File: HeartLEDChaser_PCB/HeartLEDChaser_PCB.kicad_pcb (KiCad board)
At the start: 2 copper layers, 58.8 x 52.2 mm, 35 parts, among them U1 ICM7555CBAZ, U2 CD4017BM, U3 HT7750A, U4 HX SS12F44G4

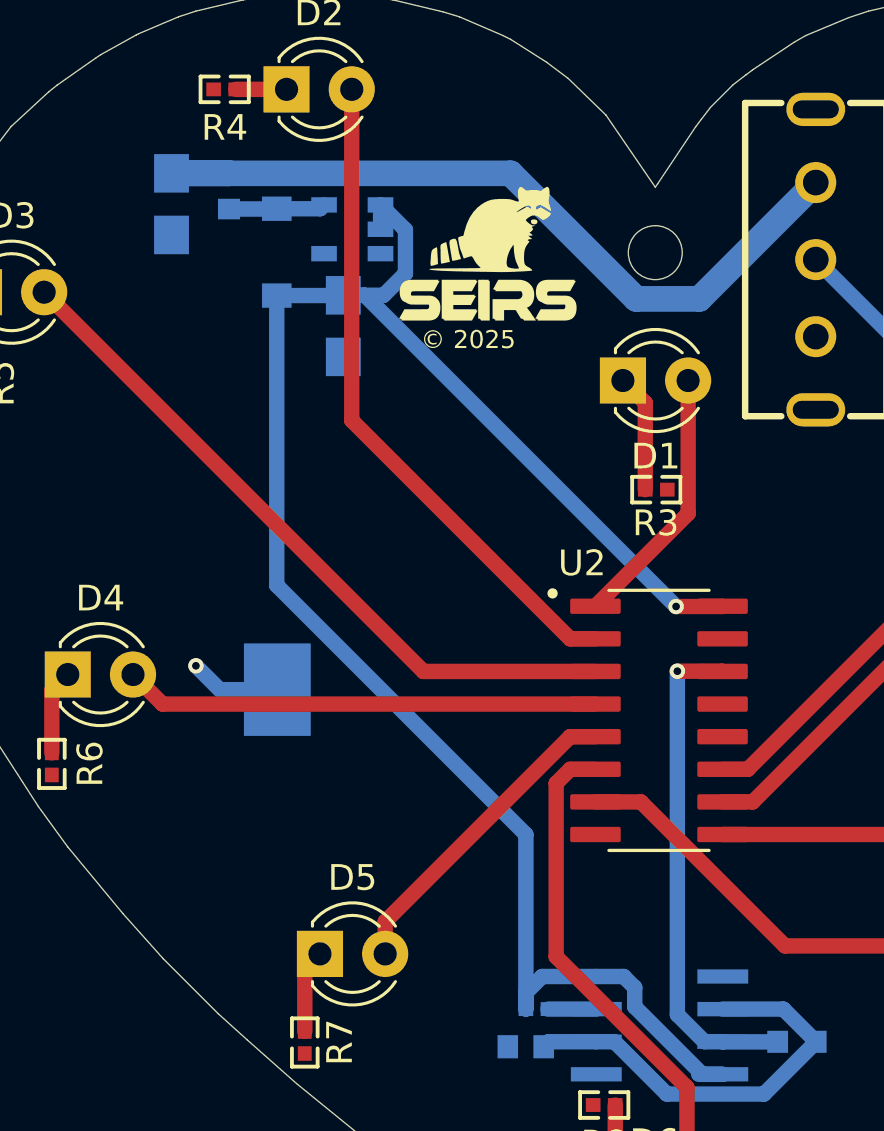
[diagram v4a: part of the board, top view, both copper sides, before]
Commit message: Corrected capacitor references
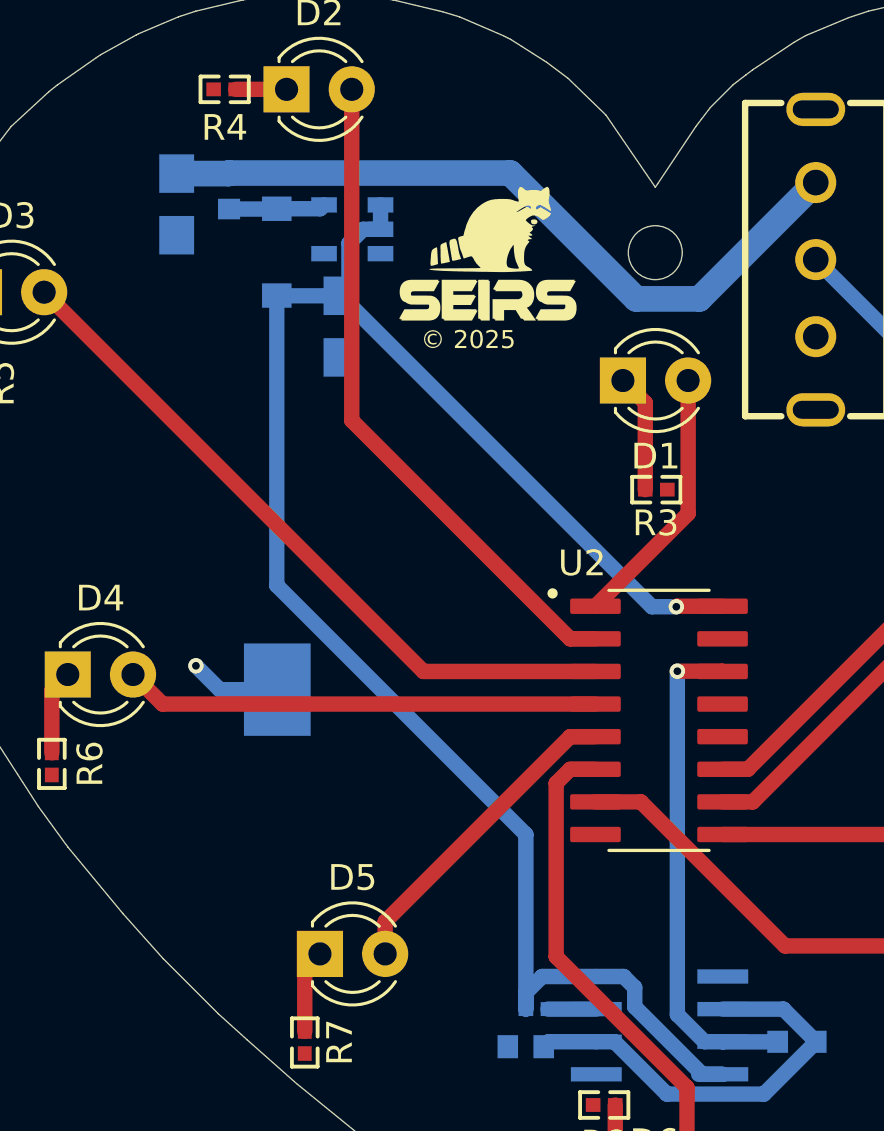
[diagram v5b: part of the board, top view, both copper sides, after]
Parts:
- removed C4: 22uF(Tantalum), FOOTPRINTS:TAJA476K006RNJ
- added C2: 47uF(Tantalum), FOOTPRINTS:TAJA476K006RNJ, B.Cu at (111.4, 80.7)
- C3: value 47uF(Tantalum) -> 22uF(Tantalum)
- moved C3 8.14 mm to (117.8, 85.5)
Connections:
- C3 pad 1: +3V0 -> +5V
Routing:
- net +3V0: track 31.2 -> 28.8 mm
- net +5V: track 72.5 -> 70.3 mm
- net Net-(D5-K): track 3.26 -> 2.43 mm
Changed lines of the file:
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@@
 	(footprint "FOOTPRINTS:TAJA476K006RNJ"
 		(layer "B.Cu")
-		(at 111.16 80.71 -90)
-		(property "Reference" "C3"
-			(at -0.01 1.64 -90)
+		(at 111.36 80.72 -90)
+		(property "Reference" "C2"
+			(at -0.01 1.69 90)
 			(layer "B.SilkS")
 			(effects
@@
 		)
 	)
-	(footprint "FOOTPRINTS:TAJA476K006RNJ"
-		(layer "B.Cu")
-		(at 117.85 85.46 -90)
-		(property "Reference" "C4"
-			(at 2.92 0.02 0)
-			(layer "B.SilkS")
-			(effects
-				(font
-					(size 1 1)
-					(thickness 0.15)
-				)
-				(justify mirror)
-			)
-		)
-		(property "Value" "22uF(Tantalum)"
-			(at 0 -4 90)
-			(layer "B.Fab")
-			(effects
-				(font
-					(size 1 1)
-					(thickness 0.15)
-				)
-				(justify mirror)
-			)
-		)
-		(property "Footprint" "FOOTPRINTS:TAJA476K006RNJ"
-			(at 0 0 90)
-			(layer "B.Fab")
-			(hide yes)
-			(effects
-				(font
-					(size 1.27 1.27)
-					(thickness 0.15)
-				)
-				(justify mirror)
-			)
-		)
-		(property "Datasheet" ""
-			(at 0 0 90)
-			(layer "B.Fab")
-			(hide yes)
-			(effects
-				(font
-					(size 1.27 1.27)
-					(thickness 0.15)
-				)
-				(justify mirror)
-			)
-		)
-		(property "Description" "Polarized capacitor"
-			(at 0 0 90)
-			(layer "B.Fab")
-			(hide yes)
-			(effects
-				(font
-					(size 1.27 1.27)
-					(thickness 0.15)
-				)
-				(justify mirror)
-			)
-		)
-		(property ki_fp_filters "CP_*")
-		(sheetname "Root")
-		(sheetfile "HeartLEDChaser_PCB.kicad_sch")
-		(attr smd)
-		(fp_line
-			(start -0.32 0.8)
-			(end -0.32 -0.8)
-			(stroke
-				(width 0.08)
-				(type solid)
-			)
-			(layer "B.SilkS")
-		)
-		(fp_line
-			(start 1.6 0.8)
-			(end -1.6 0.8)
-			(stroke
-				(width 0.08)
-				(type solid)
-			)
-			(layer "B.SilkS")
-		)
-		(fp_line
-			(start 1.57 -0.8)
-			(end -1.58 -0.8)
-			(stroke
-				(width 0.08)
-				(type solid)
-			)
-			(layer "B.SilkS")
-		)
-		(fp_circle
-			(center -1.6 -0.8)
-			(end -1.57 -0.8)
-			(stroke
-				(width 0.06)
-				(type solid)
-			)
-			(fill none)
-			(layer "B.Fab")
-		)
-		(fp_text user "${REFERENCE}"
-			(at 0 0 90)
-			(layer "B.Fab")
-			(effects
-				(font
-					(size 1 1)
-					(thickness 0.15)
-				)
-				(justify mirror)
-			)
-		)
-		(pad "1" smd rect
-			(at -1.2 0 270)
-			(size 1.5 1.36)
-			(layers "B.Cu" "B.Paste" "B.Mask")
-			(net 34 "+5V")
-			(pintype "passive")
-		)
-		(pad "2" smd rect
-			(at 1.2 0 270)
-			(size 1.5 1.36)
-			(layers "B.Cu" "B.Paste" "B.Mask")
-			(net 2 "GND")
-			(pintype "passive")
-		)
-		(model "${EASYEDA2KICAD}/easyeda2kicad.3dshapes/CASE-A_L3.2-W1.6-H1.6.wrl"
-			(offset
-				(xyz -0 -0 -0)
-			)
-			(scale
-				(xyz 1 1 1)
-			)
-			(rotate
-				(xyz 0 0 0)
-			)
-		)
-	)
 	(footprint "FOOTPRINTS:CL10A475KP8NNNC"
 		(layer "B.Cu")
@@
 		)
 	)
+	(footprint "FOOTPRINTS:TAJA476K006RNJ"
+		(layer "B.Cu")
+		(at 117.76 85.48 -90)
+		(property "Reference" "C3"
+			(at 2.84 -0.03 180)
+			(layer "B.SilkS")
+			(effects
+				(font
+					(size 1 1)
+					(thickness 0.15)
+				)
+				(justify mirror)
+			)
+		)
+		(property "Value" "22uF(Tantalum)"
+			(at 0 -4 90)
+			(layer "B.Fab")
+			(effects
+				(font
+					(size 1 1)
+					(thickness 0.15)
+				)
+				(justify mirror)
+			)
+		)
+		(property "Footprint" "FOOTPRINTS:TAJA476K006RNJ"
+			(at 0 0 90)
+			(layer "B.Fab")
+			(hide yes)
+			(effects
+				(font
+					(size 1.27 1.27)
+					(thickness 0.15)
+				)
+				(justify mirror)
+			)
+		)
+		(property "Datasheet" ""
+			(at 0 0 90)
+			(layer "B.Fab")
+			(hide yes)
+			(effects
+				(font
+					(size 1.27 1.27)
+					(thickness 0.15)
+				)
+				(justify mirror)
+			)
+		)
+		(property "Description" "Polarized capacitor"
+			(at 0 0 90)
+			(layer "B.Fab")
+			(hide yes)
+			(effects
+				(font
+					(size 1.27 1.27)
+					(thickness 0.15)
+				)
+				(justify mirror)
+			)
+		)
+		(property ki_fp_filters "CP_*")
+		(sheetname "Root")
+		(sheetfile "HeartLEDChaser_PCB.kicad_sch")
+		(attr smd)
+		(fp_line
+			(start -0.32 0.8)
+			(end -0.32 -0.8)
+			(stroke
+				(width 0.08)
+				(type solid)
+			)
+			(layer "B.SilkS")
+		)
+		(fp_line
+			(start 1.6 0.8)
+			(end -1.6 0.8)
+			(stroke
+				(width 0.08)
+				(type solid)
+			)
+			(layer "B.SilkS")
+		)
+		(fp_line
+			(start 1.57 -0.8)
+			(end -1.58 -0.8)
+			(stroke
+				(width 0.08)
+				(type solid)
+			)
+			(layer "B.SilkS")
+		)
+		(fp_circle
+			(center -1.6 -0.8)
+			(end -1.57 -0.8)
+			(stroke
+				(width 0.06)
+				(type solid)
+			)
+			(fill none)
+			(layer "B.Fab")
+		)
+		(fp_text user "${REFERENCE}"
+			(at 0 0 90)
+			(layer "B.Fab")
+			(effects
+				(font
+					(size 1 1)
+					(thickness 0.15)
+				)
+				(justify mirror)
+			)
+		)
+		(pad "1" smd rect
+			(at -1.2 0 270)
+			(size 1.5 1.36)
+			(layers "B.Cu" "B.Paste" "B.Mask")
+			(net 34 "+5V")
+			(pintype "passive")
+		)
+		(pad "2" smd rect
+			(at 1.2 0 270)
+			(size 1.5 1.36)
+			(layers "B.Cu" "B.Paste" "B.Mask")
+			(net 2 "GND")
+			(pintype "passive")
+		)
+		(model "${EASYEDA2KICAD}/easyeda2kicad.3dshapes/CASE-A_L3.2-W1.6-H1.6.wrl"
+			(offset
+				(xyz -0 -0 -0)
+			)
+			(scale
+				(xyz 1 1 1)
+			)
+			(rotate
+				(xyz 0 0 0)
+			)
+		)
+	)
 	(footprint "FOOTPRINTS:ICM7555CBAZ"
 		(layer "B.Cu")
@@
 	)
 	(segment
-		(start 113.39 79.51)
+		(start 113.38 79.52)
 		(end 113.4 79.5)
 		(width 1)
@@
 	)
 	(segment
-		(start 111.16 79.51)
-		(end 124.364416 79.51)
+		(start 131.72 84.4)
+		(end 136.25 79.87)
 		(width 1)
 		(layer "B.Cu")
@@
 	)
 	(segment
-		(start 111.16 79.51)
-		(end 113.39 79.51)
+		(start 113.4 79.5)
+		(end 124.354416 79.5)
 		(width 1)
 		(layer "B.Cu")
@@
 	)
 	(segment
-		(start 124.364416 79.51)
+		(start 124.354416 79.5)
 		(end 129.254416 84.4)
 		(width 1)
@@
 	)
 	(segment
-		(start 131.72 84.4)
-		(end 136.25 79.87)
+		(start 111.36 79.52)
+		(end 113.38 79.52)
 		(width 1)
 		(layer "B.Cu")
@@
 	)
 	(segment
-		(start 116.35 110.5)
-		(end 116.94 109.91)
-		(width 0.6)
-		(layer "F.Cu")
-		(net 5)
-	)
-	(segment
 		(start 131.28 92.76)
 		(end 131.28 87.58)
@@
 	)
 	(segment
-		(start 132.61 96.38)
-		(end 132.62 96.37)
+		(start 130.84 96.37)
+		(end 130.82 96.39)
 		(width 0.6)
 		(layer "F.Cu")
@@
 	)
 	(segment
-		(start 130.81 96.38)
-		(end 132.61 96.38)
+		(start 132.62 96.37)
+		(end 130.84 96.37)
 		(width 0.6)
 		(layer "F.Cu")
@@
 	)
 	(via
-		(at 130.81 96.38)
+		(at 130.82 96.39)
 		(size 0.6)
 		(drill 0.3)
 		(layers "F.Cu" "B.Cu")
-		(remove_unused_layers yes)
-		(keep_end_layers yes)
 		(free yes)
-		(zone_layer_connections)
 		(net 34)
 	)
 	(segment
-		(start 129.200001 111.220001)
-		(end 129.200001 111.970001)
+		(start 118.62 81.69)
+		(end 119.3 81.69)
+		(width 0.6)
+		(layer "B.Cu")
+		(net 34)
+	)
+	(segment
+		(start 119.3 81.69)
+		(end 119.3 80.74)
 		(width 0.6)
 		(layer "B.Cu")
@@
 	)
 	(segment
-		(start 118.69 84.26)
-		(end 130.81 96.38)
+		(start 129.200001 111.220001)
+		(end 129.200001 111.970001)
 		(width 0.6)
 		(layer "B.Cu")
@@
 	)
 	(segment
-		(start 117.85 84.26)
-		(end 118.69 84.26)
+		(start 115.27 84.28)
+		(end 115.26 84.27)
 		(width 0.6)
 		(layer "B.Cu")
@@
 	)
 	(segment
-		(start 119.42 84.26)
-		(end 117.85 84.26)
+		(start 129.87 96.39)
+		(end 117.76 84.28)
 		(width 0.6)
 		(layer "B.Cu")
@@
 	)
 	(segment
-		(start 120.27 81.71)
-		(end 120.27 83.41)
+		(start 118.07 83.97)
+		(end 118.07 82.24)
 		(width 0.6)
 		(layer "B.Cu")
@@
 	)
 	(segment
-		(start 119.3 80.74)
-		(end 120.27 81.71)
+		(start 118.07 82.24)
+		(end 118.62 81.69)
 		(width 0.6)
 		(layer "B.Cu")
@@
 	)
 	(segment
-		(start 115.26 84.27)
-		(end 117.84 84.27)
+		(start 117.76 84.28)
+		(end 118.07 83.97)
 		(width 0.6)
 		(layer "B.Cu")
@@
 	)
 	(segment
-		(start 119.3 80.74)
-		(end 119.3 81.69)
+		(start 117.76 84.28)
+		(end 115.27 84.28)
 		(width 0.6)
 		(layer "B.Cu")
@@
 	)
 	(segment
-		(start 129.200001 111.970001)
-		(end 131.83 114.6)
+		(start 130.82 96.39)
+		(end 129.87 96.39)
 		(width 0.6)
 		(layer "B.Cu")
@@
 	)
 	(segment
-		(start 120.27 83.41)
-		(end 119.42 84.26)
+		(start 129.200001 111.970001)
+		(end 131.83 114.6)
 		(width 0.6)
 		(layer "B.Cu")
